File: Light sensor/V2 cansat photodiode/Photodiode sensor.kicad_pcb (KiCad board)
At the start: 2 copper layers, 23 parts, among them IC1 MCP6002-E_MS, IC2 MCP6002-E_MS, J1 Conn_01x02, J2 Conn_01x05, J3 Conn_01x04

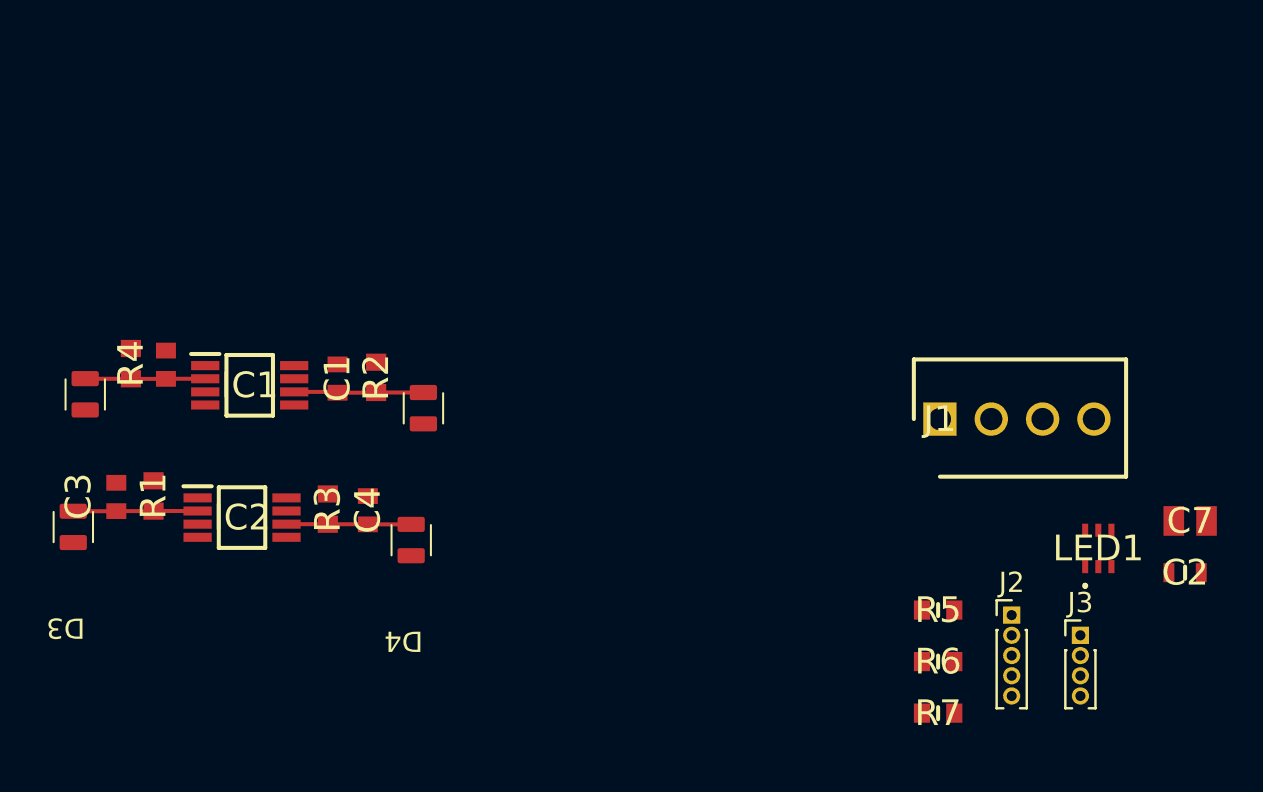
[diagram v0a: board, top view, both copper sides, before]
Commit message: Version 2 of light sensor PCB
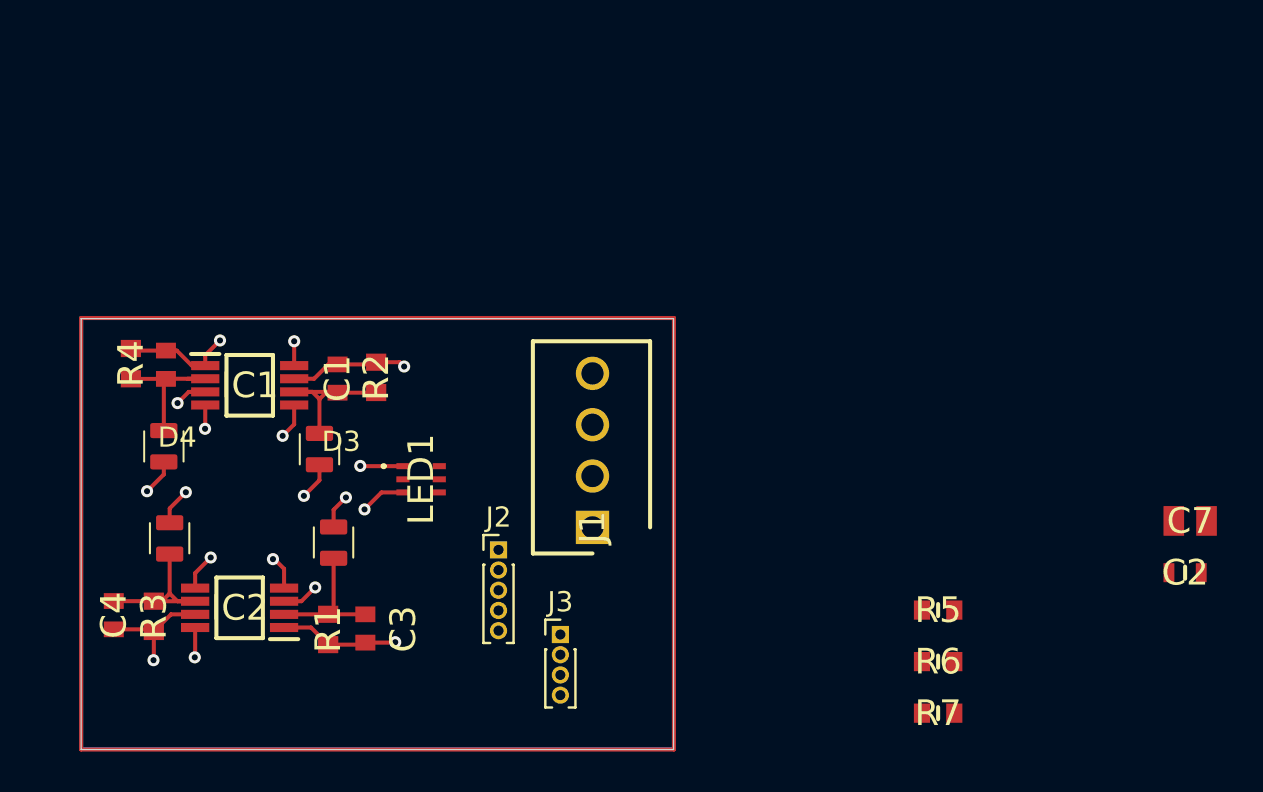
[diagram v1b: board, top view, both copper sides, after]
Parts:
- moved LED1 33.7 mm to (129.0, 76.8), turned to -90 degrees
- moved J3 25.7 mm to (135.9, 84.5)
- moved J2 25.6 mm to (132.8, 80.3)
- moved J1 18.0 mm to (137.5, 79.2), turned to 90 degrees
- moved D3 15.9 mm to (125.1, 75.5), turned to 0 degrees
- moved D4 14.4 mm to (117.0, 75.3), turned to 0 degrees
- moved C3 13.9 mm to (126.3, 84.2), turned to 90 degrees
- moved C4 13.6 mm to (113.8, 83.6), turned to -90 degrees
- moved R1 10.9 mm to (124.4, 84.3), turned to 90 degrees
- moved R3 10.1 mm to (115.8, 83.6), turned to -90 degrees
- moved D2 5.53 mm to (123.6, 79.9)
- moved D1 4.66 mm to (115.9, 79.7)
- moved IC2 4.47 mm to (120.0, 83.2), turned to 180 degrees
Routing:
- net /Out1A: track 0.00 -> 24.1 mm, vias 0 -> 1
- net /Out2B: track 0.00 -> 23.9 mm, vias 0 -> 1
- net /Out1B: track 0.04 -> 19.9 mm, vias 0 -> 1
- net GND: track 0.00 -> 19.4 mm, vias 0 -> 11
- net /Out2A: track 0.00 -> 11.7 mm, vias 0 -> 1
- net /3.3V: track 0.00 -> 4.80 mm, vias 0 -> 3
- net Net-(D4-K): track 6.17 -> 8.34 mm
- net Net-(D2-K): track 6.44 -> 7.71 mm
- net Net-(D1-K): track 5.95 -> 7.16 mm
- net Net-(D3-K): track 6.15 -> 6.92 mm
- added copper zone on B.Cu, net /3.3V
- added copper zone on In2.Cu, net /3.3V
- added copper zone on B.Cu, net GND
- added copper zone on F.Cu, net GND
- added copper zone on In1.Cu, net GND
- added copper zone on In2.Cu, net GND
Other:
- board outline added: 29.3 x 21.3 mm
- copper layers 2 -> 4

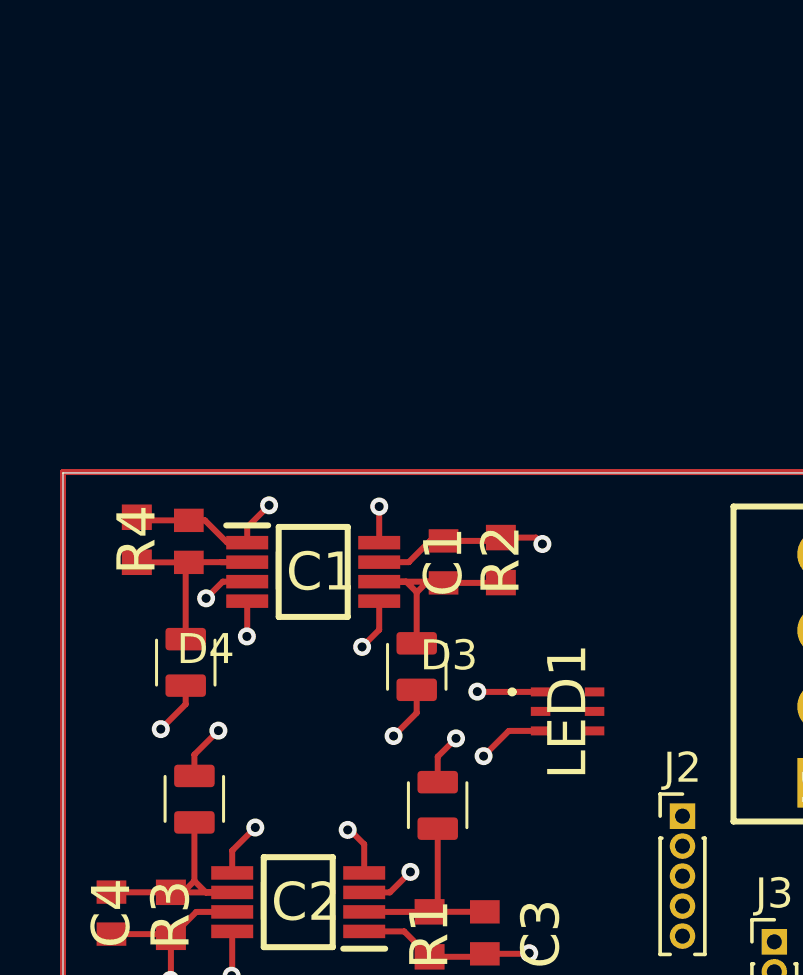
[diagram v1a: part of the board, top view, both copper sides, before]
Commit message: V3 light sensor
It is the neatest one so far. It had a lot better EMC than originally thought for the 4 channel op amp
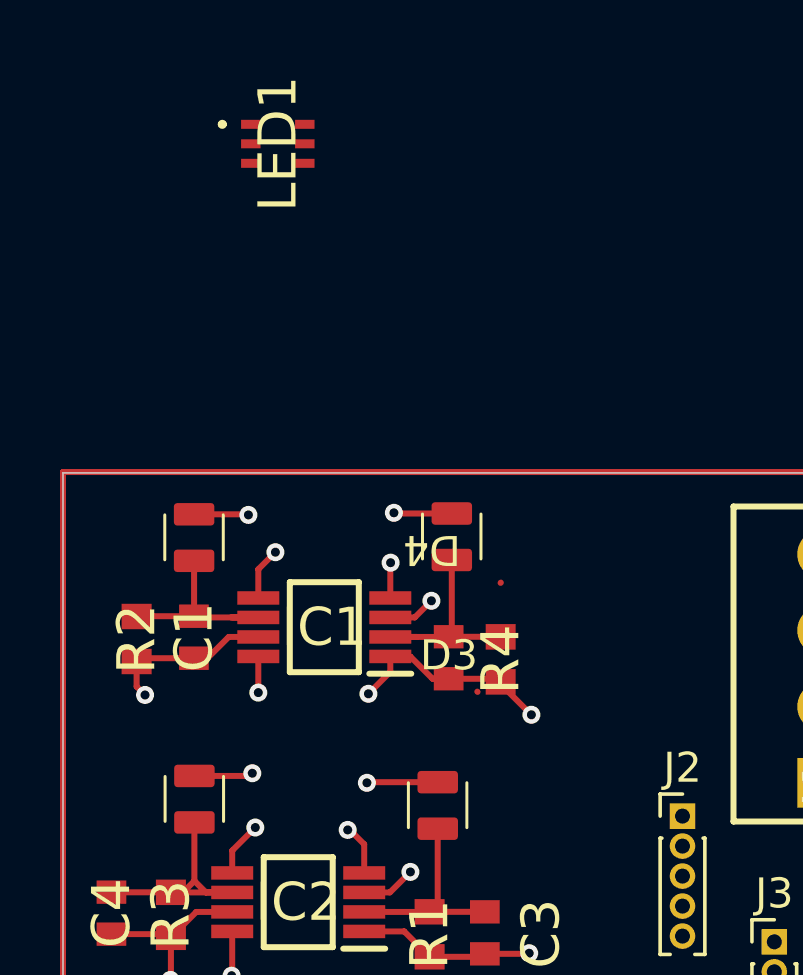
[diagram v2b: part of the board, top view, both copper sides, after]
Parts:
- moved LED1 21.2 mm to (119.4, 57.9)
- moved D1 16.3 mm to (125.5, 66.5), turned to 0 degrees
- moved D2 14.9 mm to (116.9, 66.6), turned to 0 degrees
- moved R4 12.8 mm to (126.8, 75.1), turned to 90 degrees
- moved R2 12.4 mm to (114.7, 74.4), turned to -90 degrees
- moved C8 9.49 mm to (125.1, 75.1), turned to 90 degrees
- moved C1 8.69 mm to (116.6, 74.4), turned to -90 degrees
- moved IC1 1.88 mm to (120.9, 74.0), turned to 180 degrees
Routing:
- net /Out1A: track 24.1 -> 13.9 mm, vias 1 -> 2
- net /Out1B: track 19.9 -> 26.1 mm
- net /3.3V: track 4.80 -> 2.70 mm, vias 3 -> 2
- net GND: track 19.4 -> 18.0 mm, vias 11 -> 10
- net Net-(D2-K): track 7.71 -> 6.84 mm
